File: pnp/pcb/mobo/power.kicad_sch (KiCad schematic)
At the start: 29 parts, among them J12 COMBO_POWER_JACK, U11 FDS4435BZ, U12 TPS54331, U13 AP1117-33, U6 Fuse_Holder_3568

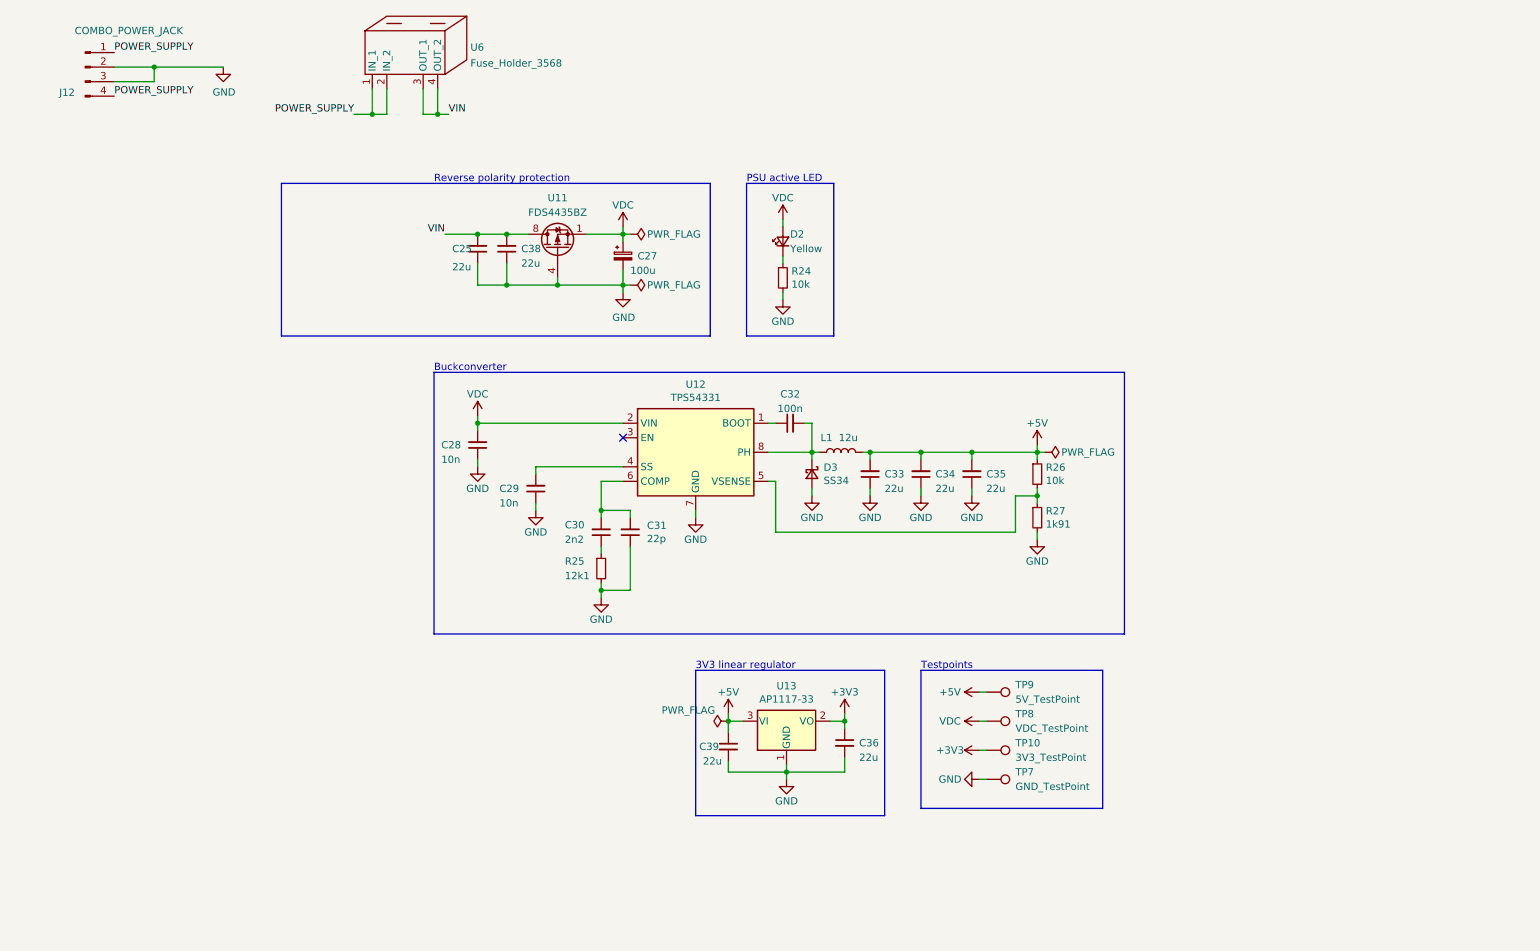
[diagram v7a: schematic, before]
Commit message: adds tons of TVS and inline resistors
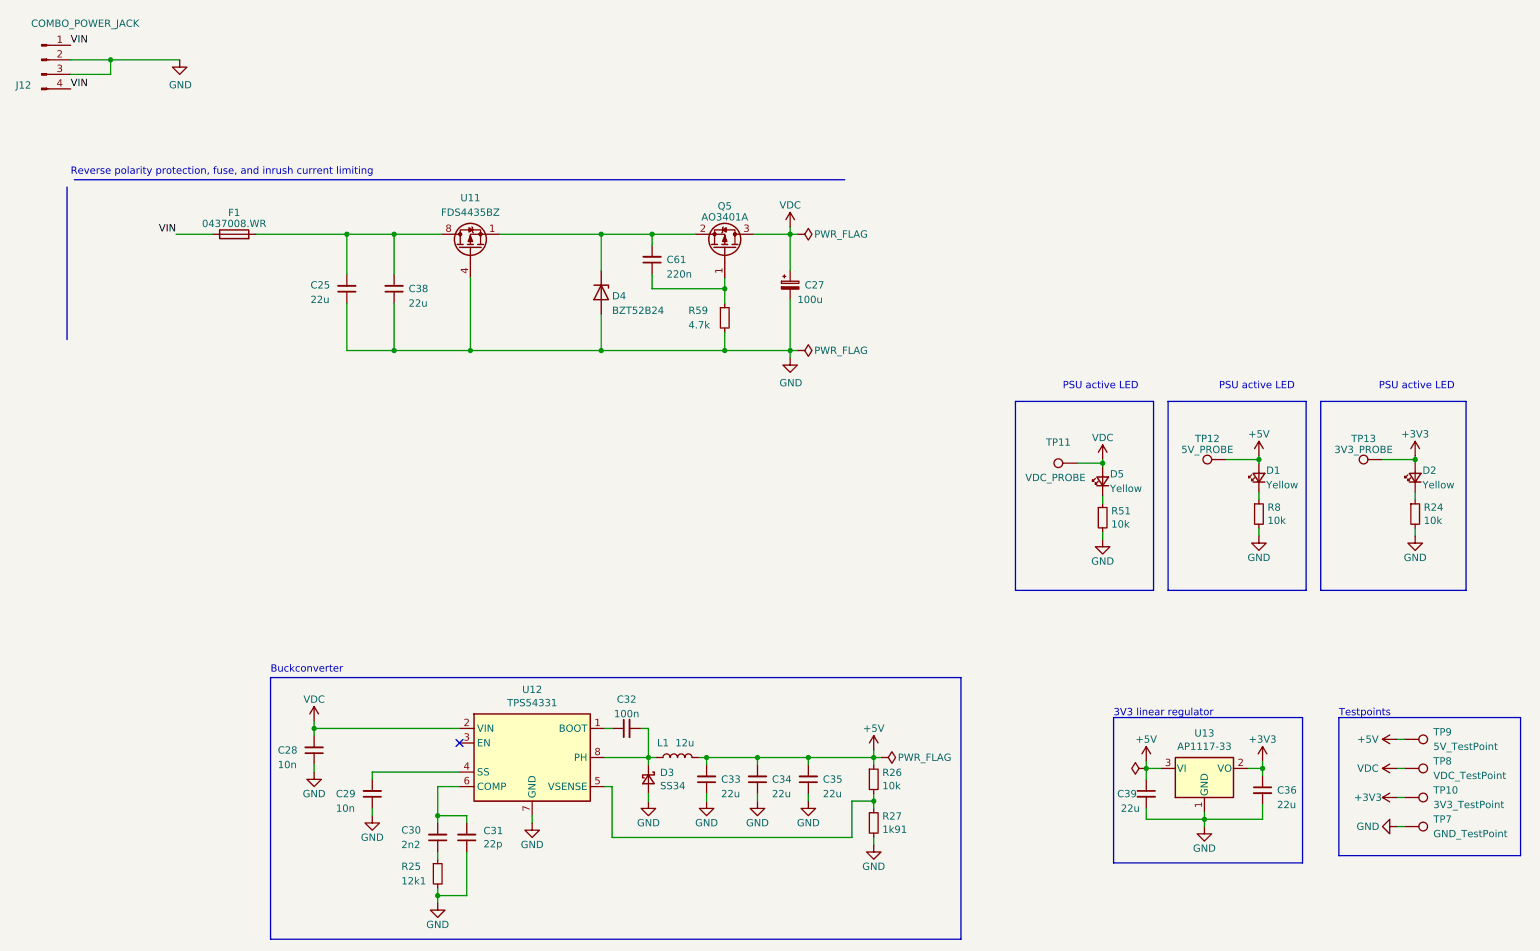
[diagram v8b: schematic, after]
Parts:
- removed U6: Fuse_Holder_3568, index:Fuse_Holder_3568, symbol index:Fuse_Holder_3568
- added C61: 220n, Capacitor_SMD:C_0805_2012Metric, symbol Device:C_Small
- added D1, D5: Yellow, LED_SMD:LED_0805_2012Metric, symbol Device:LED_Small
- added D4: BZT52B24, Diode_SMD:D_SOD-123F, symbol Diode:BZT52Bxx
- added F1: 0437008.WR, Fuse:Fuse_1206_3216Metric, symbol Device:Fuse
- added Q5: AO3401A, Package_TO_SOT_SMD:SOT-23, symbol Transistor_FET:AO3401A
- added R51, R8: 10k, Resistor_SMD:R_0805_2012Metric, symbol Device:R_Small
- added R59: 4.7k, Resistor_SMD:R_0805_2012Metric, symbol Device:R_Small
- added TP11: VDC_PROBE, TestPoint:TestPoint_THTPad_1.5x1.5mm_Drill0.7mm, symbol Connector:TestPoint
- added TP12: 5V_PROBE, TestPoint:TestPoint_THTPad_1.5x1.5mm_Drill0.7mm, symbol Connector:TestPoint
- added TP13: 3V3_PROBE, TestPoint:TestPoint_THTPad_1.5x1.5mm_Drill0.7mm, symbol Connector:TestPoint
- L1: footprint Inductor_SMD:L_Coilcraft_XAL60xx_6.36x6.56mm -> Inductor_SMD:L_Coilcraft_XAL6060-XXX
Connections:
- net POWER_SUPPLY is gone; now on net VIN: J12.1 (Pin_1), J12.4 (Pin_4)
- net +3V3: now also D2.2 (A), TP13.1
- net +5V: now also D1.2 (A), TP12.1
- net GND: now also D4.2 (A), R51.2, R59.2, R8.2
- net VDC: now also D5.2 (A), Q5.3 (D), TP11.1; no longer D2.2 (A), U11.1 (S), U11.2 (S), U11.3 (S)
- net VIN: now also F1.1; no longer C25.2, C38.2, U11.5 (D), U11.6 (D), U11.7 (D), U11.8 (D)
- new net: C61.2, D4.1 (K), Q5.2 (S), U11.1 (S), U11.2 (S), U11.3 (S)
- new net: C25.2, C38.2, F1.2, U11.5 (D), U11.6 (D), U11.7 (D), U11.8 (D)
- new net: D5.1 (K), R51.1
- new net: D1.1 (K), R8.1
- new net: C61.1, Q5.1 (G), R59.1
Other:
- note added: "Reverse polarity protection, fuse, and inrush current limiting"
- note removed: "Reverse polarity protection"
- moved on the sheet: C25, C27, C28, C29, C30, C31, C32, C33, C34, C35, C36, C38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
